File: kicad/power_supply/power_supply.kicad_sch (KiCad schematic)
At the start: 0 parts

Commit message: psu buck-boost schematic capture
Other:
- added sheet Buck-Boost (buck_boost.kicad_sch)
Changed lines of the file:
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@@
 	)
 	(sheet
-		(at 88.265 41.275)
-		(size 33.02 24.765)
+		(at 73.66 86.995)
+		(size 24.13 13.335)
 		(fields_autoplaced yes)
 		(stroke
@@
 		)
 		(property "Sheetname" "Charger"
-			(at 88.265 40.5634 0)
+			(at 73.66 86.2834 0)
 			(effects
 				(font
@@
 		)
 		(property "Sheetfile" "charger.kicad_sch"
-			(at 88.265 66.6246 0)
+			(at 73.66 100.9146 0)
 			(effects
 				(font
@@
 	)
 	(sheet
-		(at 44.45 41.275)
-		(size 32.385 24.13)
+		(at 41.275 86.995)
+		(size 24.765 13.335)
 		(fields_autoplaced yes)
 		(stroke
@@
 		)
 		(property "Sheetname" "USB-C PD"
-			(at 44.45 40.5634 0)
+			(at 41.275 86.2834 0)
 			(effects
 				(font
@@
 		)
 		(property "Sheetfile" "usb_c_pd.kicad_sch"
-			(at 44.45 65.9896 0)
+			(at 41.275 100.9146 0)
 			(effects
 				(font
@@
 		)
 		(pin "VSNK" output
-			(at 76.835 53.34 0)
+			(at 66.04 93.98 0)
 			(effects
 				(font
@@
 				)
 			)
+		)
+	)
+	(sheet
+		(at 107.95 87.63)
+		(size 25.4 13.97)
+		(fields_autoplaced yes)
+		(stroke
+			(width 0.1524)
+			(type solid)
+		)
+		(fill
+			(color 0 0 0 0.0000)
+		)
+		(property "Sheetname" "Buck-Boost"
+			(at 107.95 86.9184 0)
+			(effects
+				(font
+					(size 1.27 1.27)
+				)
+				(justify left bottom)
+			)
+		)
+		(property "Sheetfile" "buck_boost.kicad_sch"
+			(at 107.95 102.1846 0)
+			(effects
+				(font
+					(size 1.27 1.27)
+				)
+				(justify left top)
+			)
+		)
+		(property "Field2" ""
+			(at 107.95 87.63 0)
+			(effects
+				(font
+					(size 1.27 1.27)
+				)
+				(hide yes)
+			)
+		)
+		(instances
+			(project "power_supply"
+				(path "/6a7d9dc9-f78f-470f-911b-b95256023173"
+					(page "4")
+				)
+			)

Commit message: schematic capture
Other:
- sheet Buck-Boost ports: added FB_BT, VIN, VOUT; removed none
- sheet Charger ports: added VBATT, VIN, VOUT; removed none
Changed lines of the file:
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@@
 	)
 	(sheet
-		(at 73.66 86.995)
-		(size 24.13 13.335)
+		(at 82.55 62.23)
+		(size 22.86 18.415)
 		(fields_autoplaced yes)
 		(stroke
@@
 		)
 		(property "Sheetname" "Charger"
-			(at 73.66 86.2834 0)
+			(at 82.55 61.5184 0)
 			(effects
 				(font
@@
 		)
 		(property "Sheetfile" "charger.kicad_sch"
-			(at 73.66 100.9146 0)
+			(at 82.55 81.2296 0)
 			(effects
 				(font
@@
 				)
 				(justify left top)
+			)
+		)
+		(pin "VIN" input
+			(at 82.55 71.12 180)
+			(effects
+				(font
+					(size 1.27 1.27)
+				)
+				(justify left)
+			)
+		)
+		(pin "VBATT" bidirectional
+			(at 105.41 76.2 0)
+			(effects
+				(font
+					(size 1.27 1.27)
+				)
+				(justify right)
+			)
+		)
+		(pin "VOUT" output
+			(at 105.41 67.31 0)
+			(effects
+				(font
+					(size 1.27 1.27)
+				)
+				(justify right)
 			)
 		)
@@
 	)
 	(sheet
-		(at 41.275 86.995)
-		(size 24.765 13.335)
+		(at 44.45 63.5)
+		(size 24.13 15.875)
 		(fields_autoplaced yes)
 		(stroke
@@
 		)
 		(property "Sheetname" "USB-C PD"
-			(at 41.275 86.2834 0)
+			(at 44.45 62.7884 0)
 			(effects
 				(font
@@
 		)
 		(property "Sheetfile" "usb_c_pd.kicad_sch"
-			(at 41.275 100.9146 0)
+			(at 44.45 79.9596 0)
 			(effects
 				(font
@@
 		)
 		(pin "VSNK" output
-			(at 66.04 93.98 0)
+			(at 68.58 71.12 0)
 			(effects
 				(font
@@
 	)
 	(sheet
-		(at 107.95 87.63)
-		(size 25.4 13.97)
+		(at 119.38 58.42)
+		(size 25.4 18.415)
 		(fields_autoplaced yes)
 		(stroke
@@
 		)
 		(property "Sheetname" "Buck-Boost"
-			(at 107.95 86.9184 0)
+			(at 119.38 57.7084 0)
 			(effects
 				(font
@@
 		)
 		(property "Sheetfile" "buck_boost.kicad_sch"
-			(at 107.95 102.1846 0)
+			(at 119.38 77.4196 0)
 			(effects
 				(font
@@
 		)
 		(property "Field2" ""
-			(at 107.95 87.63 0)
+			(at 119.38 58.42 0)
 			(effects
 				(font
@@
 			)
 		)
+		(pin "VIN" input
+			(at 119.38 67.31 180)
+			(effects
+				(font
+					(size 1.27 1.27)
+				)
+				(justify left)
+			)
+		)
+		(pin "VOUT" output
+			(at 144.78 63.5 0)
+			(effects
+				(font
+					(size 1.27 1.27)
+				)
+				(justify right)
+			)
+		)
+		(pin "FB_BT" input
+			(at 144.78 72.39 0)
+			(effects
+				(font
+					(size 1.27 1.27)
+				)
+				(justify right)
+			)
+		)

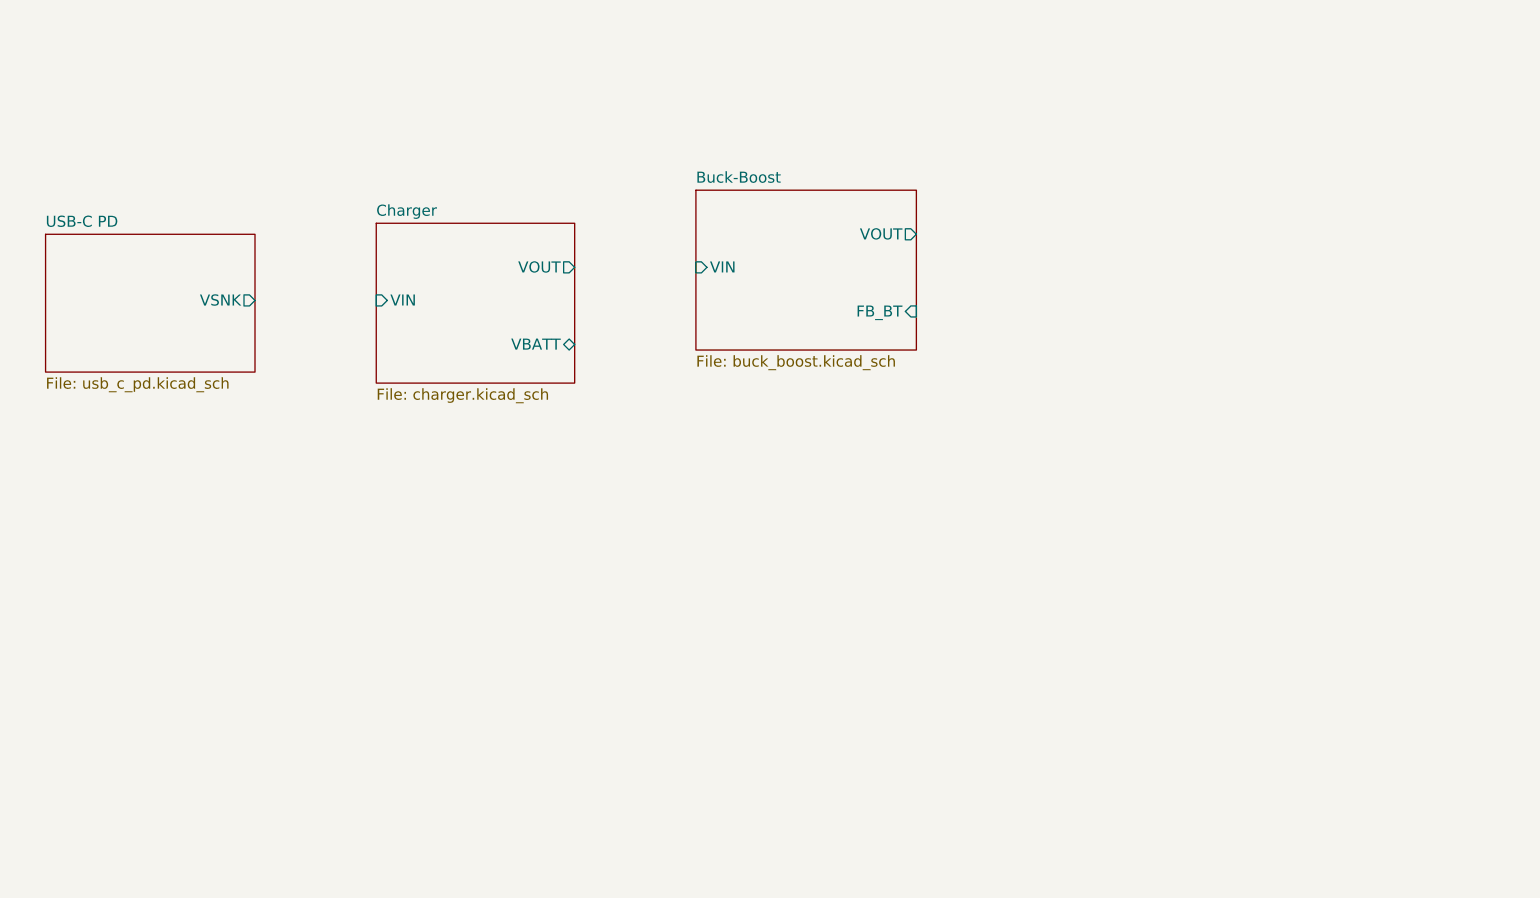
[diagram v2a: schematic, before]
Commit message: improved load switch mosfet paste aperture
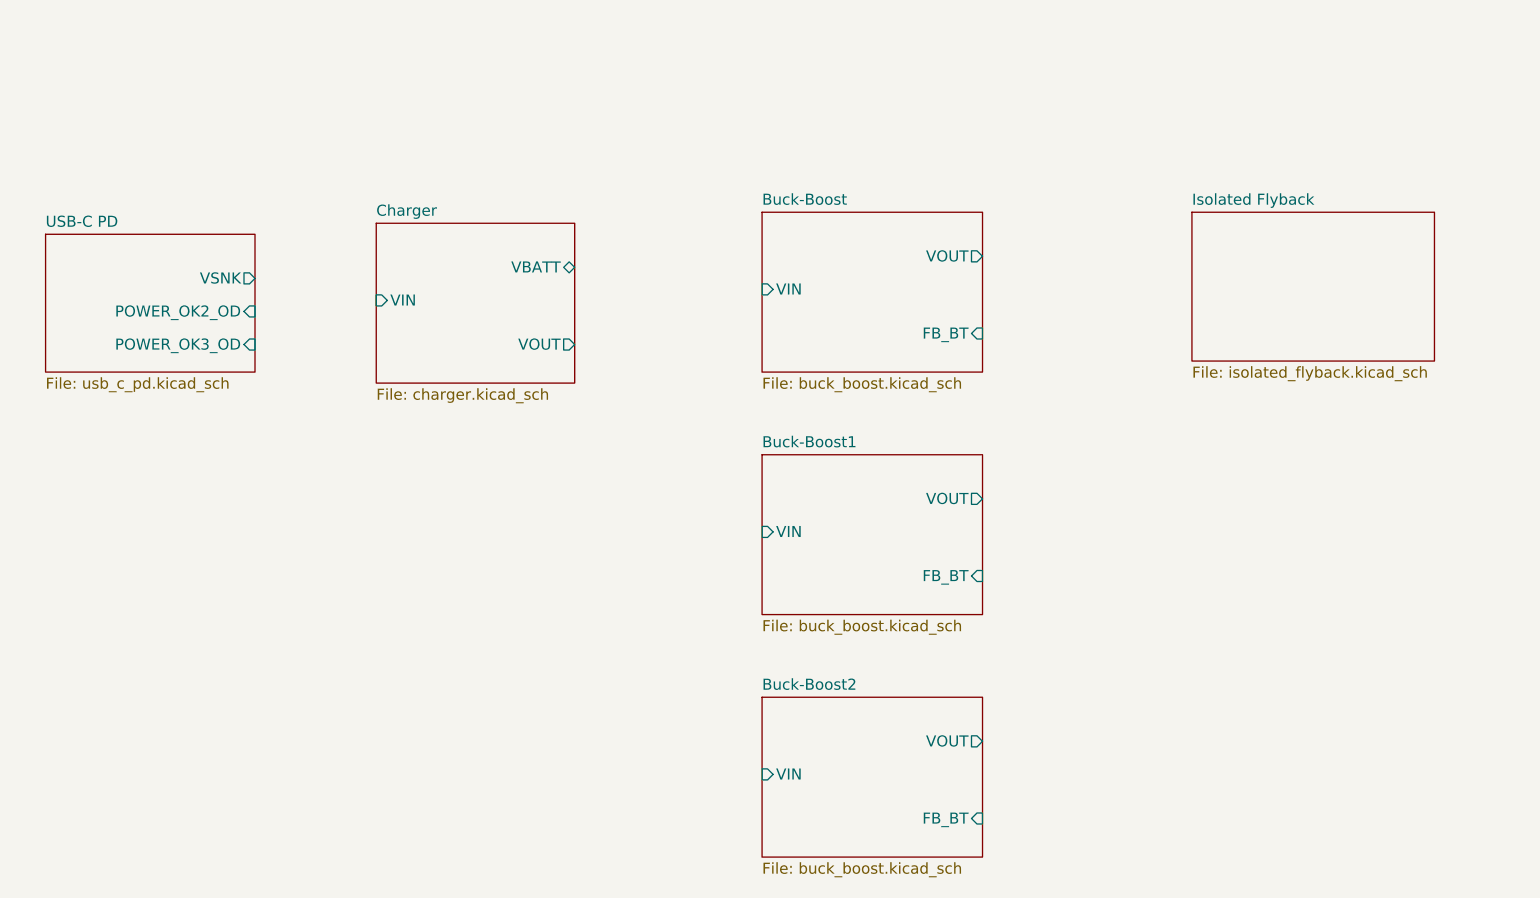
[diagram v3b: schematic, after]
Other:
- added sheet Buck-Boost1 (buck_boost.kicad_sch)
- added sheet Buck-Boost2 (buck_boost.kicad_sch)
- added sheet Isolated Flyback (isolated_flyback.kicad_sch)
- sheet USB-C PD ports: added POWER_OK2_OD, POWER_OK3_OD; removed none
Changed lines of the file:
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@@
 		)
 		(pin "VBATT" bidirectional
+			(at 105.41 67.31 0)
+			(effects
+				(font
+					(size 1.27 1.27)
+				)
+				(justify right)
+			)
+		)
+		(pin "VOUT" output
 			(at 105.41 76.2 0)
 			(effects
@@
 			)
 		)
-		(pin "VOUT" output
-			(at 105.41 67.31 0)
-			(effects
-				(font
-					(size 1.27 1.27)
-				)
-				(justify right)
-			)
-		)
 		(instances
 			(project "power_supply"
 				(path "/6a7d9dc9-f78f-470f-911b-b95256023173"
 					(page "3")
+				)
+			)
+		)
+	)
+	(sheet
+		(at 176.53 60.96)
+		(size 27.94 17.145)
+		(fields_autoplaced yes)
+		(stroke
+			(width 0.1524)
+			(type solid)
+		)
+		(fill
+			(color 0 0 0 0.0000)
+		)
+		(property "Sheetname" "Isolated Flyback"
+			(at 176.53 60.2484 0)
+			(effects
+				(font
+					(size 1.27 1.27)
+				)
+				(justify left bottom)
+			)
+		)
+		(property "Sheetfile" "isolated_flyback.kicad_sch"
+			(at 176.53 78.6896 0)
+			(effects
+				(font
+					(size 1.27 1.27)
+				)
+				(justify left top)
+			)
+		)
+		(instances
+			(project "power_supply"
+				(path "/6a7d9dc9-f78f-470f-911b-b95256023173"
+					(page "7")
 				)
 			)
@@
 		)
 		(pin "VSNK" output
-			(at 68.58 71.12 0)
+			(at 68.58 68.58 0)
+			(effects
+				(font
+					(size 1.27 1.27)
+				)
+				(justify right)
+			)
+		)
+		(pin "POWER_OK3_OD" input
+			(at 68.58 76.2 0)
+			(effects
+				(font
+					(size 1.27 1.27)
+				)
+				(justify right)
+			)
+		)
+		(pin "POWER_OK2_OD" input
+			(at 68.58 72.39 0)
 			(effects
 				(font
@@
 	)
 	(sheet
-		(at 119.38 58.42)
+		(at 127 116.84)
 		(size 25.4 18.415)
 		(fields_autoplaced yes)
@@
 			(color 0 0 0 0.0000)
 		)
+		(property "Sheetname" "Buck-Boost2"
+			(at 127 116.1284 0)
+			(effects
+				(font
+					(size 1.27 1.27)
+				)
+				(justify left bottom)
+			)
+		)
+		(property "Sheetfile" "buck_boost.kicad_sch"
+			(at 127 135.8396 0)
+			(effects
+				(font
+					(size 1.27 1.27)
+				)
+				(justify left top)
+			)
+		)
+		(property "Field2" ""
+			(at 127 116.84 0)
+			(effects
+				(font
+					(size 1.27 1.27)
+				)
+				(hide yes)
+			)
+		)
+		(pin "VIN" input
+			(at 127 125.73 180)
+			(effects
+				(font
+					(size 1.27 1.27)
+				)
+				(justify left)
+			)
+		)
+		(pin "VOUT" output
+			(at 152.4 121.92 0)
+			(effects
+				(font
+					(size 1.27 1.27)
+				)
+				(justify right)
+			)
+		)
+		(pin "FB_BT" input
+			(at 152.4 130.81 0)
+			(effects
+				(font
+					(size 1.27 1.27)
+				)
+				(justify right)
+			)
+		)
+		(instances
+			(project "power_supply"
+				(path "/6a7d9dc9-f78f-470f-911b-b95256023173"
+					(page "6")
+				)
+			)
+		)
+	)
+	(sheet
+		(at 127 60.96)
+		(size 25.4 18.415)
+		(fields_autoplaced yes)
+		(stroke
+			(width 0.1524)
+			(type solid)
+		)
+		(fill
+			(color 0 0 0 0.0000)
+		)
 		(property "Sheetname" "Buck-Boost"
-			(at 119.38 57.7084 0)
+			(at 127 60.2484 0)
 			(effects
 				(font
@@
 		)
 		(property "Sheetfile" "buck_boost.kicad_sch"
-			(at 119.38 77.4196 0)
+			(at 127 79.9596 0)
 			(effects
 				(font
@@
 		)
 		(property "Field2" ""
-			(at 119.38 58.42 0)
+			(at 127 60.96 0)
 			(effects
 				(font
@@
 		)
 		(pin "VIN" input
-			(at 119.38 67.31 180)
+			(at 127 69.85 180)
 			(effects
 				(font
@@
 		)
 		(pin "VOUT" output
-			(at 144.78 63.5 0)
+			(at 152.4 66.04 0)
 			(effects
 				(font
@@
 		)
 		(pin "FB_BT" input
-			(at 144.78 72.39 0)
+			(at 152.4 74.93 0)
 			(effects
 				(font
@@
 				)
 			)
+		)
+	)
+	(sheet
+		(at 127 88.9)
+		(size 25.4 18.415)
+		(fields_autoplaced yes)
+		(stroke
+			(width 0.1524)
+			(type solid)
+		)
+		(fill
+			(color 0 0 0 0.0000)
+		)
+		(property "Sheetname" "Buck-Boost1"
+			(at 127 88.1884 0)
+			(effects
+				(font
+					(size 1.27 1.27)
+				)
+				(justify left bottom)
+			)
+		)
+		(property "Sheetfile" "buck_boost.kicad_sch"
+			(at 127 107.8996 0)
+			(effects
+				(font
+					(size 1.27 1.27)
+				)
+				(justify left top)
+			)
+		)
+		(property "Field2" ""
+			(at 127 88.9 0)
+			(effects
+				(font
+					(size 1.27 1.27)
+				)
+				(hide yes)
+			)
+		)
+		(pin "VIN" input
+			(at 127 97.79 180)
+			(effects
+				(font
+					(size 1.27 1.27)
+				)
+				(justify left)
+			)
+		)
+		(pin "VOUT" output
+			(at 152.4 93.98 0)
+			(effects
+				(font
+					(size 1.27 1.27)
+				)
+				(justify right)
+			)
+		)
+		(pin "FB_BT" input
+			(at 152.4 102.87 0)
+			(effects
+				(font
+					(size 1.27 1.27)
+				)
+				(justify right)
+			)
+		)
+		(instances
+			(project "power_supply"
+				(path "/6a7d9dc9-f78f-470f-911b-b95256023173"
+					(page "5")
+				)
+			)
